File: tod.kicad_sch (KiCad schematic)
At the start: 65 parts, among them J1 Conn_01x04, J2 Conn_01x03, J3 Conn_01x04, J4 Conn_01x03, Q1 BC856B, Q2 BC817, Q3 BC856B, Q4 BC817, Q5 BC856, Q6 BC817, Q7 BC856, Q8 BC817, U1 PC817, U2 PC817, U3 PC817, U4 PC817

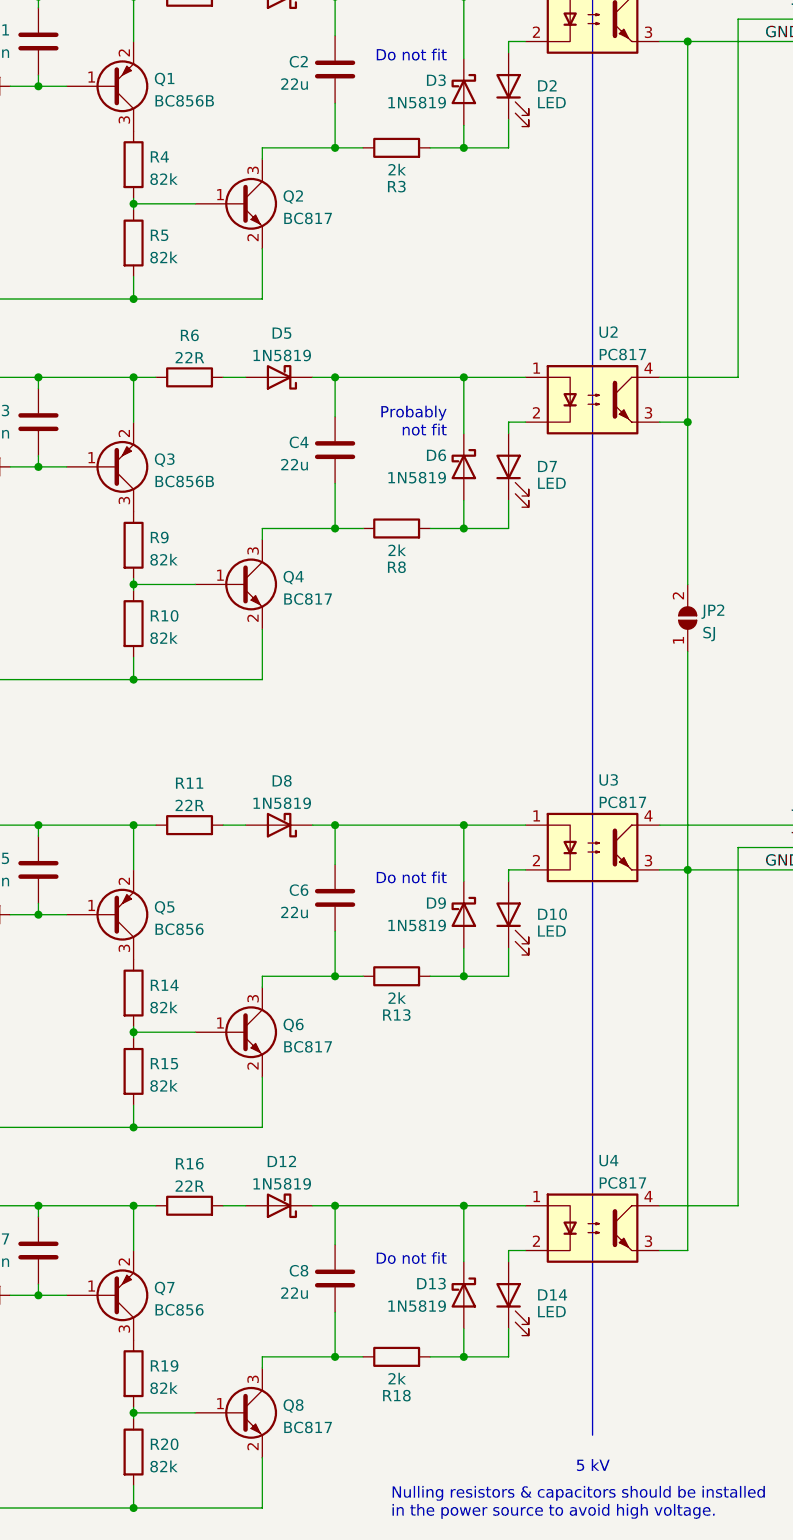
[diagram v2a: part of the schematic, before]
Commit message: Revert "Use 2k resistors instead of 3k9."
This reverts commit e4b48c20f046feec0504172c1823d5e465362b53.
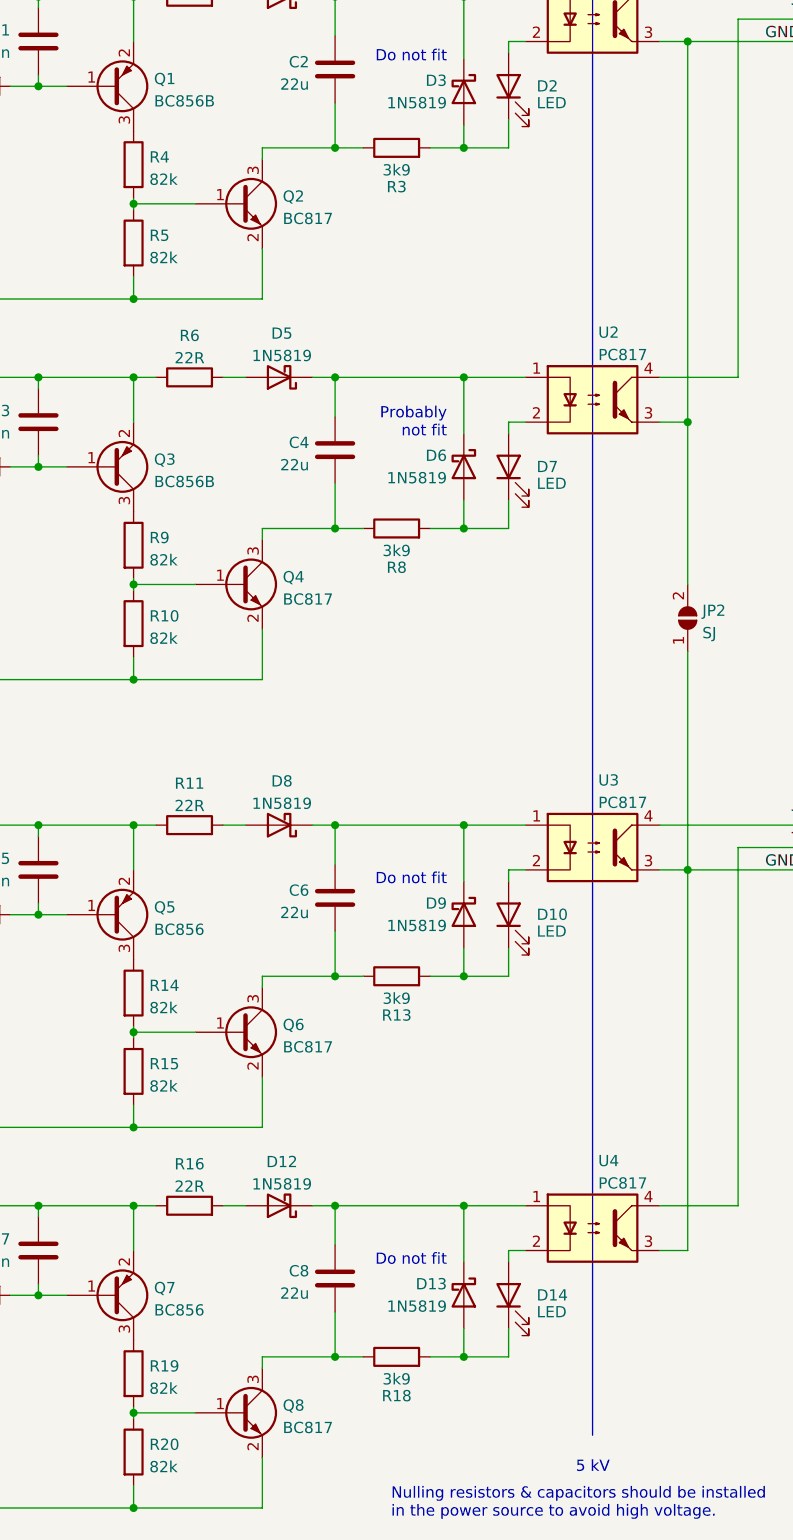
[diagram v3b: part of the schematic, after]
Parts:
- R13, R18, R3, R8: value 2k -> 3k9; LCSC C17604 -> C17614
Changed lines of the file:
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@@
   (symbol (lib_id "Graphic:Logo_Open_Hardware_Small") (at 275.082 157.988 0) (unit 1)
     (in_bom yes) (on_board yes) (fields_autoplaced)
-    (property "Reference" "#LOGO1" (id 0) (at 275.082 151.003 0)
+    (property "Reference" "#LOGO?" (id 0) (at 275.082 151.003 0)
       (effects (font (size 1.27 1.27)) hide)
     )
@@
     (in_bom yes) (on_board yes)
     (property "Reference" "R3" (id 0) (at 123.825 43.18 90))
-    (property "Value" "2k" (id 1) (at 123.825 41.275 90))
+    (property "Value" "3k9" (id 1) (at 123.825 41.275 90))
     (property "Footprint" "Resistor_SMD:R_0805_2012Metric_Pad1.20x1.40mm_HandSolder" (id 2) (at 123.825 40.513 90)
       (effects (font (size 1.27 1.27)) hide)
@@
       (effects (font (size 1.27 1.27)) hide)
     )
-    (property "LCSC" "C17604" (id 4) (at 123.825 38.735 0)
+    (property "LCSC" "C17614" (id 4) (at 123.825 38.735 0)
       (effects (font (size 1.27 1.27)) hide)
     )
@@
     (in_bom yes) (on_board yes)
     (property "Reference" "R8" (id 0) (at 123.825 86.36 90))
-    (property "Value" "2k" (id 1) (at 123.825 84.455 90))
+    (property "Value" "3k9" (id 1) (at 123.825 84.455 90))
     (property "Footprint" "Resistor_SMD:R_0805_2012Metric_Pad1.20x1.40mm_HandSolder" (id 2) (at 123.825 83.693 90)
       (effects (font (size 1.27 1.27)) hide)
@@
       (effects (font (size 1.27 1.27)) hide)
     )
-    (property "LCSC" "C17604" (id 4) (at 123.825 81.915 0)
+    (property "LCSC" "C17614" (id 4) (at 123.825 81.915 0)
       (effects (font (size 1.27 1.27)) hide)
     )
@@
     (in_bom yes) (on_board yes)
     (property "Reference" "R18" (id 0) (at 123.825 180.34 90))
-    (property "Value" "2k" (id 1) (at 123.825 178.435 90))
+    (property "Value" "3k9" (id 1) (at 123.825 178.435 90))
     (property "Footprint" "Resistor_SMD:R_0805_2012Metric_Pad1.20x1.40mm_HandSolder" (id 2) (at 123.825 177.673 90)
       (effects (font (size 1.27 1.27)) hide)
@@
       (effects (font (size 1.27 1.27)) hide)
     )
-    (property "LCSC" "C17604" (id 4) (at 123.825 175.895 0)
+    (property "LCSC" "C17614" (id 4) (at 123.825 175.895 0)
       (effects (font (size 1.27 1.27)) hide)
     )
@@
     (in_bom yes) (on_board yes)
     (property "Reference" "R13" (id 0) (at 123.825 137.16 90))
-    (property "Value" "2k" (id 1) (at 123.825 135.255 90))
+    (property "Value" "3k9" (id 1) (at 123.825 135.255 90))
     (property "Footprint" "Resistor_SMD:R_0805_2012Metric_Pad1.20x1.40mm_HandSolder" (id 2) (at 123.825 134.493 90)
       (effects (font (size 1.27 1.27)) hide)
@@
       (effects (font (size 1.27 1.27)) hide)
     )
-    (property "LCSC" "C17604" (id 4) (at 123.825 132.715 0)
+    (property "LCSC" "C17614" (id 4) (at 123.825 132.715 0)
       (effects (font (size 1.27 1.27)) hide)
     )
@@
   (symbol_instances
     (path "/361cc21e-47c7-4d2d-b684-c4ecf46e1791"
-      (reference "#LOGO1") (unit 1) (value "Logo_Open_Hardware_Small") (footprint "")
+      (reference "#LOGO?") (unit 1) (value "Logo_Open_Hardware_Small") (footprint "")
     )
     (path "/949e12d6-32f4-4bfa-9bdc-0a2dc68d9702"
@@
     )
     (path "/6482a8d5-54ad-47be-8272-081fe112eec4"
-      (reference "R3") (unit 1) (value "2k") (footprint "Resistor_SMD:R_0805_2012Metric_Pad1.20x1.40mm_HandSolder")
+      (reference "R3") (unit 1) (value "3k9") (footprint "Resistor_SMD:R_0805_2012Metric_Pad1.20x1.40mm_HandSolder")
     )
     (path "/78c42f87-2789-4e07-b18d-8f8b5409a989"
@@
     )
     (path "/ad5e9409-abbd-41d0-a4a7-824ec612606c"
-      (reference "R8") (unit 1) (value "2k") (footprint "Resistor_SMD:R_0805_2012Metric_Pad1.20x1.40mm_HandSolder")
+      (reference "R8") (unit 1) (value "3k9") (footprint "Resistor_SMD:R_0805_2012Metric_Pad1.20x1.40mm_HandSolder")
     )
     (path "/03771697-dfea-4597-9909-b3909b334a64"
@@
     )
     (path "/f08c1b46-15a3-4269-a58c-f504dad3ff5c"
-      (reference "R13") (unit 1) (value "2k") (footprint "Resistor_SMD:R_0805_2012Metric_Pad1.20x1.40mm_HandSolder")
+      (reference "R13") (unit 1) (value "3k9") (footprint "Resistor_SMD:R_0805_2012Metric_Pad1.20x1.40mm_HandSolder")
     )
     (path "/c7861c30-7054-427f-b1e2-1f003c1d4aa4"
@@
     )
     (path "/b4d0cd47-ee70-4cd4-921c-1bfdb9da9a6f"
-      (reference "R18") (unit 1) (value "2k") (footprint "Resistor_SMD:R_0805_2012Metric_Pad1.20x1.40mm_HandSolder")
+      (reference "R18") (unit 1) (value "3k9") (footprint "Resistor_SMD:R_0805_2012Metric_Pad1.20x1.40mm_HandSolder")
     )
     (path "/54f5c2ae-e7ec-4883-ab5a-237e9f7ba07b"

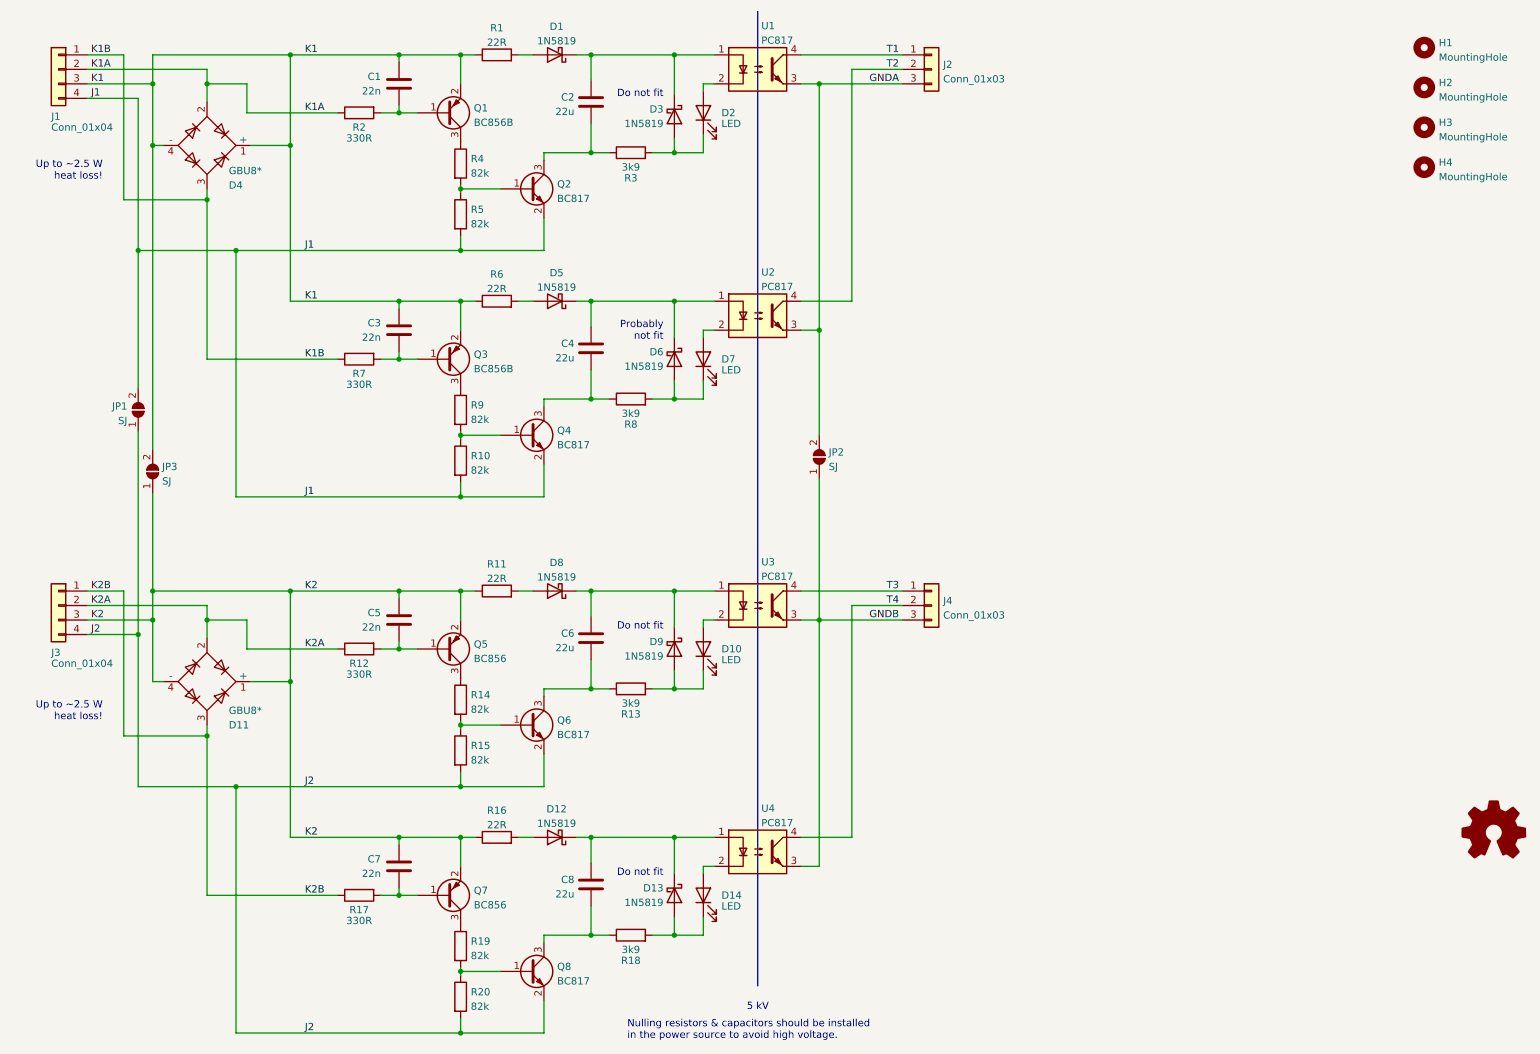
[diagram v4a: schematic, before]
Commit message: Use screw terminals schematics mark insted of generic connector.
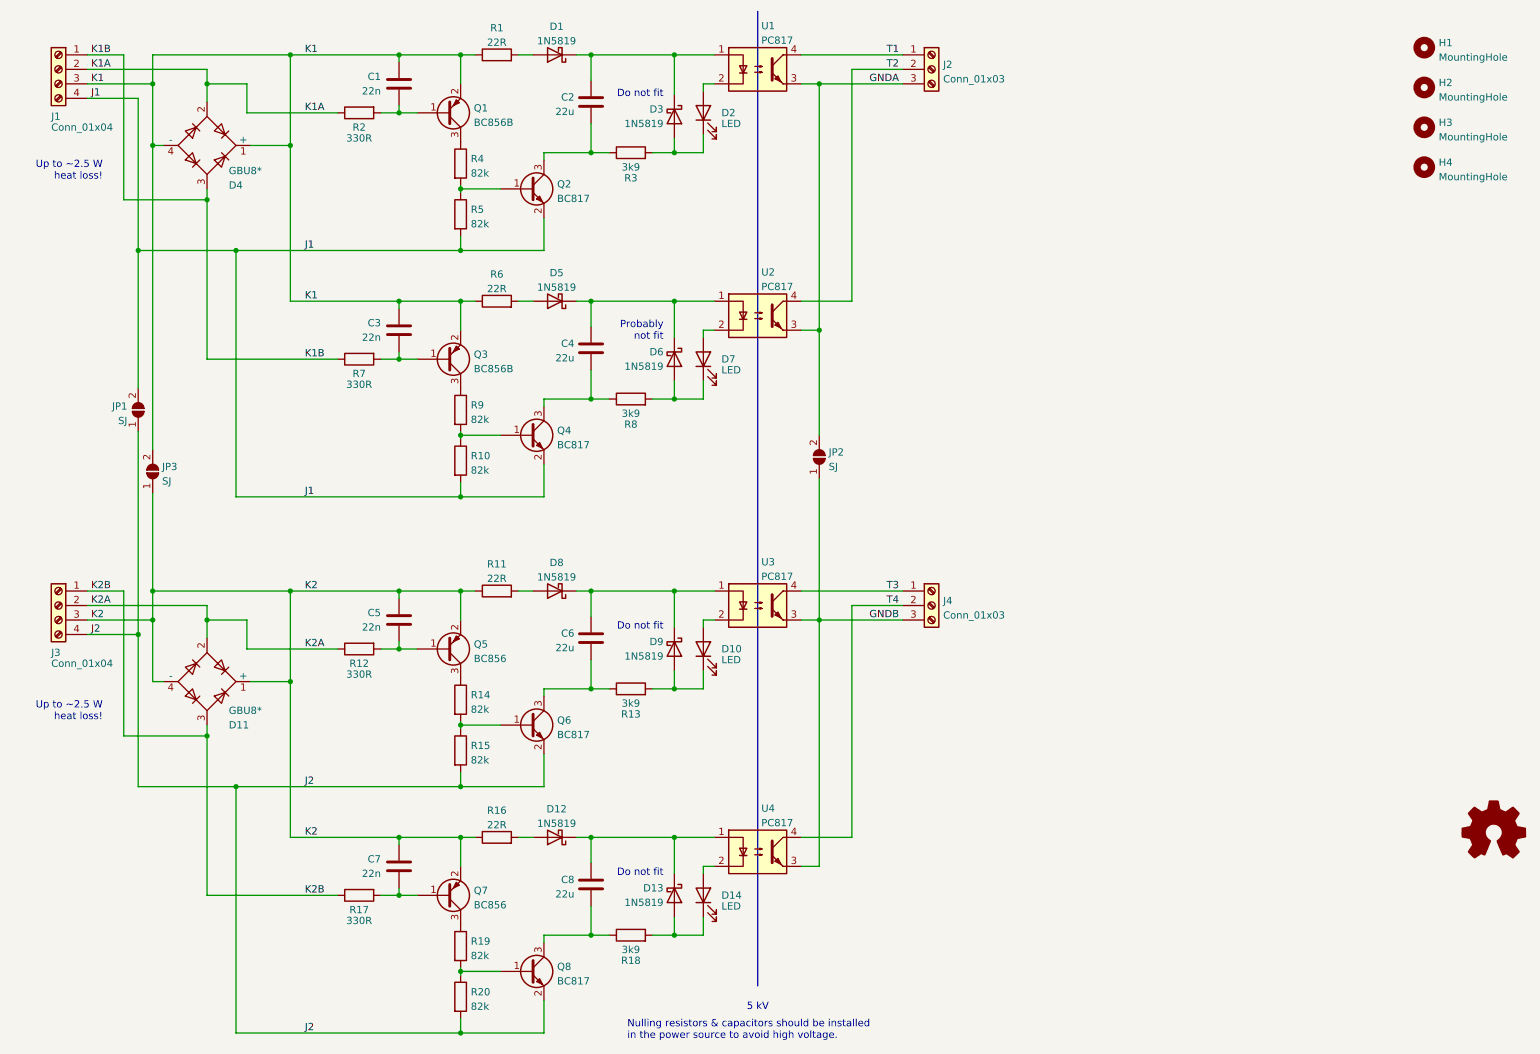
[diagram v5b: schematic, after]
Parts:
- J1, J3: symbol Connector_Generic:Conn_01x04 -> Connector:Screw_Terminal_01x04
- J2, J4: symbol Connector_Generic:Conn_01x03 -> Connector:Screw_Terminal_01x03
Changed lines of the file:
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@@
     (pin "2")
   )
-  (symbol (lib_id "Connector_Generic:Conn_01x03") (at 176.53 24.13 0) (unit 1)
+  (symbol (lib_id "Connector:Screw_Terminal_01x03") (at 176.53 24.13 0) (unit 1)
     (in_bom yes) (on_board yes) (fields_autoplaced)
     (property "Reference" "J2" (id 0) (at 178.562 23.2953 0)
@@
     (pin "3")
   )
-  (symbol (lib_id "Connector_Generic:Conn_01x03") (at 176.53 118.11 0) (unit 1)
+  (symbol (lib_id "Connector:Screw_Terminal_01x03") (at 176.53 118.11 0) (unit 1)
     (in_bom yes) (on_board yes) (fields_autoplaced)
     (property "Reference" "J4" (id 0) (at 178.562 117.2753 0)
@@
     (pin "3")
   )
-  (symbol (lib_id "Connector_Generic:Conn_01x04") (at 23.495 118.11 0) (mirror y) (unit 1)
+  (symbol (lib_id "Connector:Screw_Terminal_01x04") (at 23.495 118.11 0) (mirror y) (unit 1)
     (in_bom yes) (on_board yes)
     (property "Reference" "J3" (id 0) (at 22.225 126.365 0)
@@
     (pin "2")
   )
-  (symbol (lib_id "Connector_Generic:Conn_01x04") (at 23.495 24.13 0) (mirror y) (unit 1)
+  (symbol (lib_id "Connector:Screw_Terminal_01x04") (at 23.495 24.13 0) (mirror y) (unit 1)
     (in_bom yes) (on_board yes)
     (property "Reference" "J1" (id 0) (at 22.225 32.385 0)

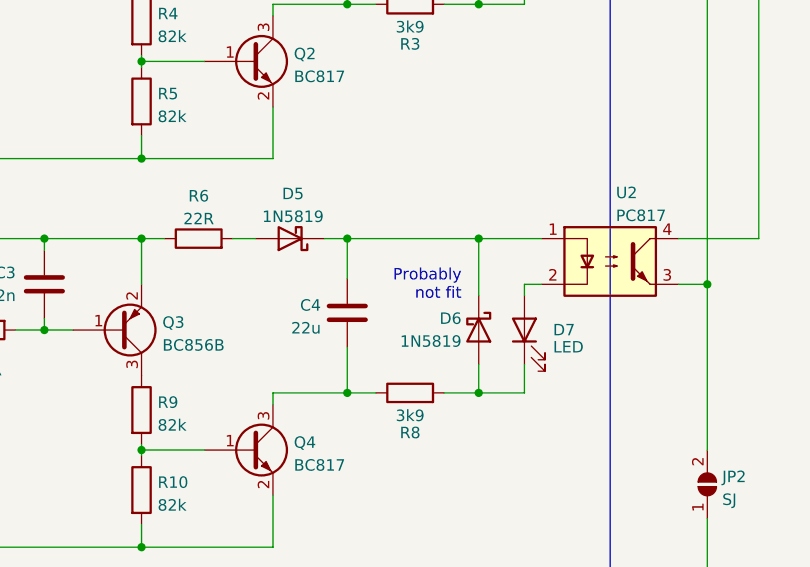
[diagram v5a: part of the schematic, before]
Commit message: Fix inconsistent text.
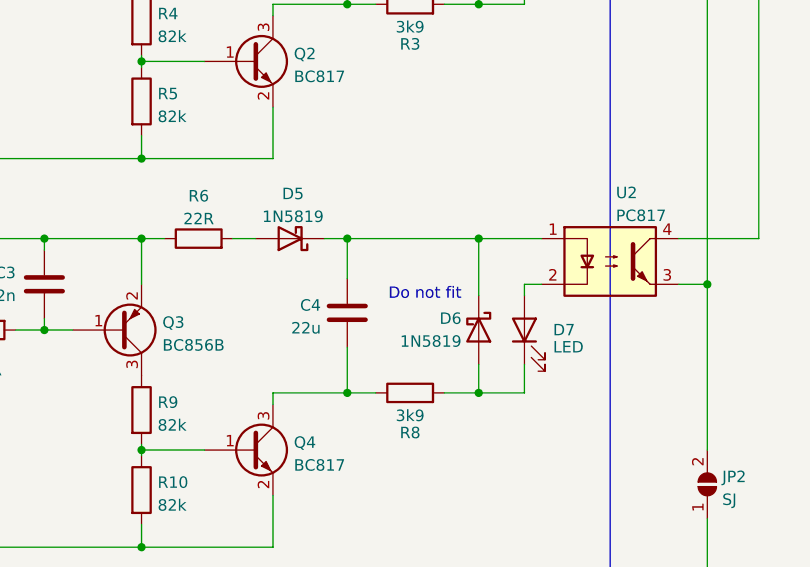
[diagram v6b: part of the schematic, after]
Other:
- note removed: "Probably not fit"
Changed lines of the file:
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@@
     (effects (font (size 1.27 1.27)) (justify right bottom))
   )
-  (text "Probably\nnot fit" (at 129.54 71.755 180)
+  (text "Do not fit" (at 129.54 71.755 180)
     (effects (font (size 1.27 1.27)) (justify right bottom))
   )
